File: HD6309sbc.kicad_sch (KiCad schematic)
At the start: 23 parts, among them J1 Conn_01x02_Male, J2 Conn_02x30_Odd_Even, J3 Conn_01x02_Male, U1 HD63C09, U10 74HC375, U11 74HC02, U12 74HC21, U13 74HC21, U4 UM61256FK, U5 UM61256FK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

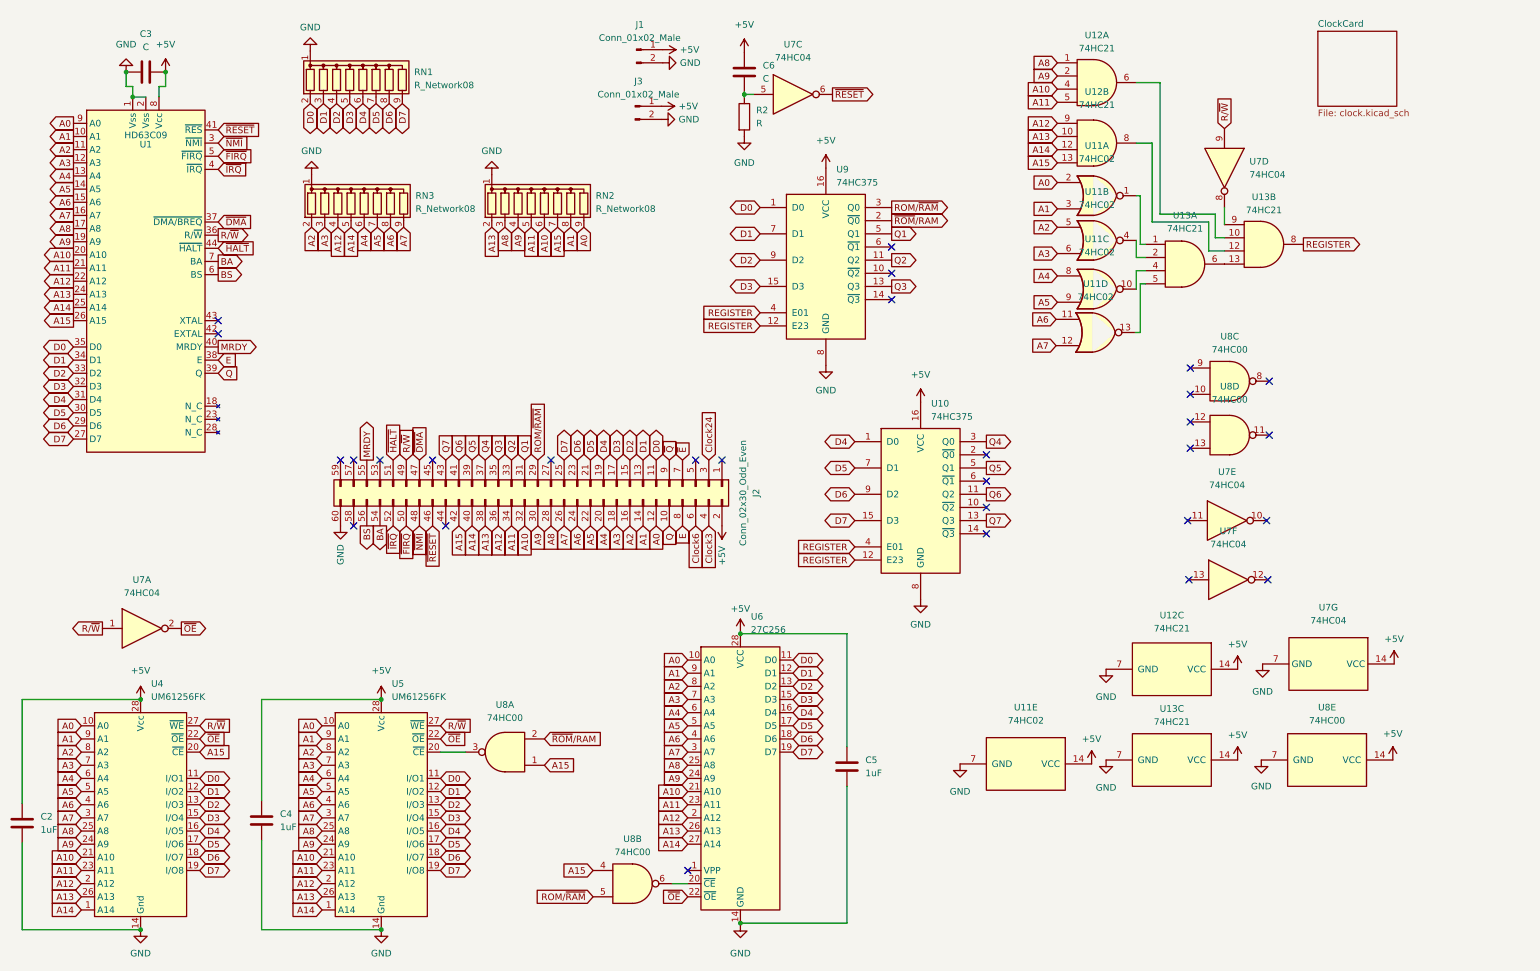
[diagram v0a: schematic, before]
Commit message: add paged memory
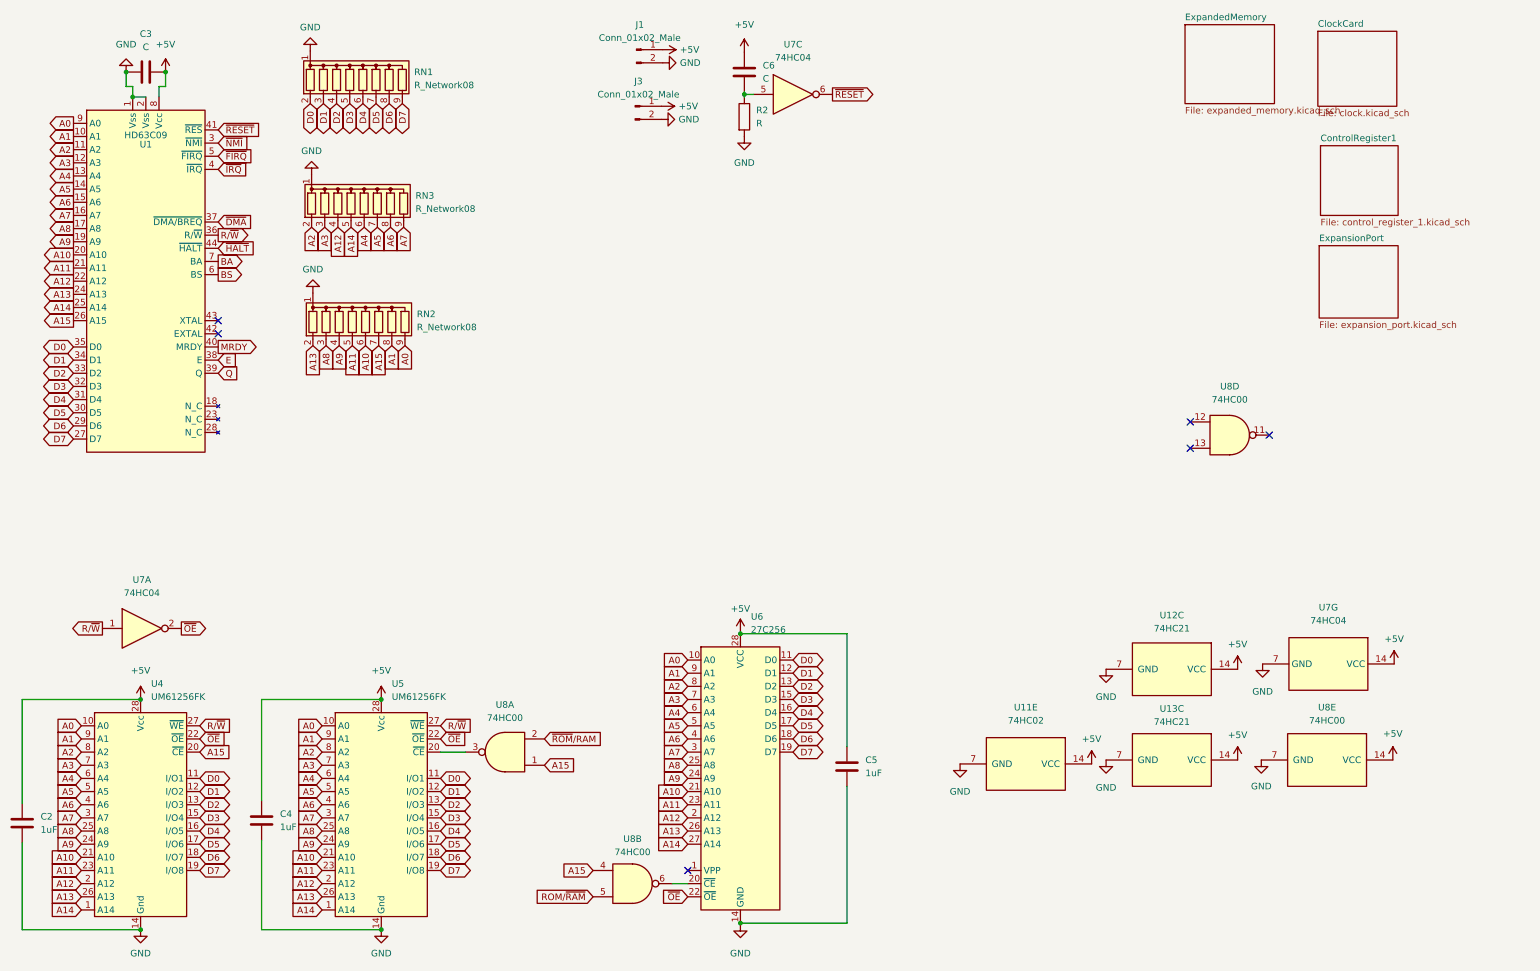
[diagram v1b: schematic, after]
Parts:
- removed J2: Conn_02x30_Odd_Even, Connector_PinHeader_2.54mm:PinHeader_2x30_P2.54mm_Vertical, symbol Connector_Generic:Conn_02x30_Odd_Even
- removed U10, U9: 74HC375, Package_SO:SO-16_3.9x9.9mm_P1.27mm, symbol 74xx:74LS375
- removed unit 4 of U11
- removed unit 3 of U11
- removed unit 1 of U11
- removed unit 2 of U11
- removed unit 1 of U12
- removed unit 2 of U12
- removed unit 2 of U13
- removed unit 1 of U13
- removed unit 5 of U7
- removed unit 6 of U7
- removed unit 4 of U7
- removed unit 3 of U8
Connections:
- no-connect marks 29 -> 6
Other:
- added sheet ControlRegister1 (control_register_1.kicad_sch)
- added sheet ExpandedMemory (expanded_memory.kicad_sch)
- added sheet ExpansionPort (expansion_port.kicad_sch)
- moved on the sheet: RN2

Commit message: add power routing
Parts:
- C3: value C -> 1uF

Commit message: rearrange components for routing
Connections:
- net A0: now also RN3.2 (R1); no longer RN2.9 (R8)
- net A1: now also RN3.3 (R2); no longer RN2.8 (R7)
- net A10: now also RN2.7 (R6); no longer RN2.6 (R5)
- net A11: now also RN2.6 (R5); no longer RN2.5 (R4)
- net A12: now also RN2.5 (R4); no longer RN3.4 (R3)
- net A13: now also RN2.4 (R3); no longer RN2.2 (R1)
- net A14: now also RN2.3 (R2); no longer RN3.5 (R4)
- net A15: now also RN2.2 (R1); no longer RN2.7 (R6)
- net A2: now also RN3.4 (R3); no longer RN3.2 (R1)
- net A3: now also RN3.5 (R4); no longer RN3.3 (R2)
- net A8: now also RN2.9 (R8); no longer RN2.3 (R2)
- net A9: now also RN2.8 (R7); no longer RN2.4 (R3)

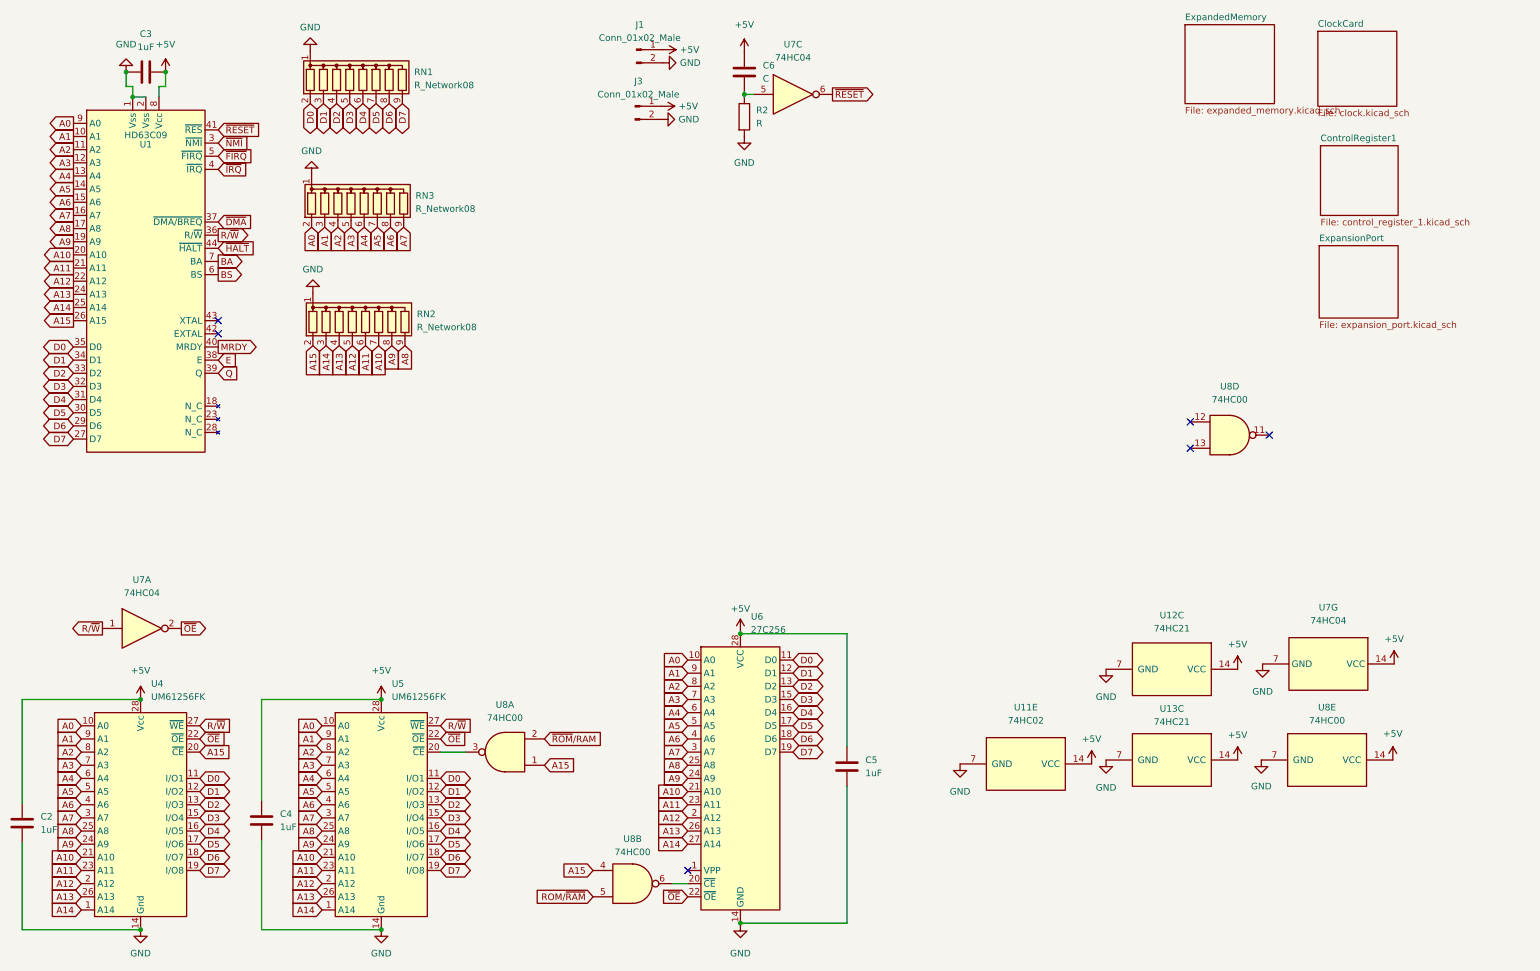
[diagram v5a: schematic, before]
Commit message: move paged memory to external board
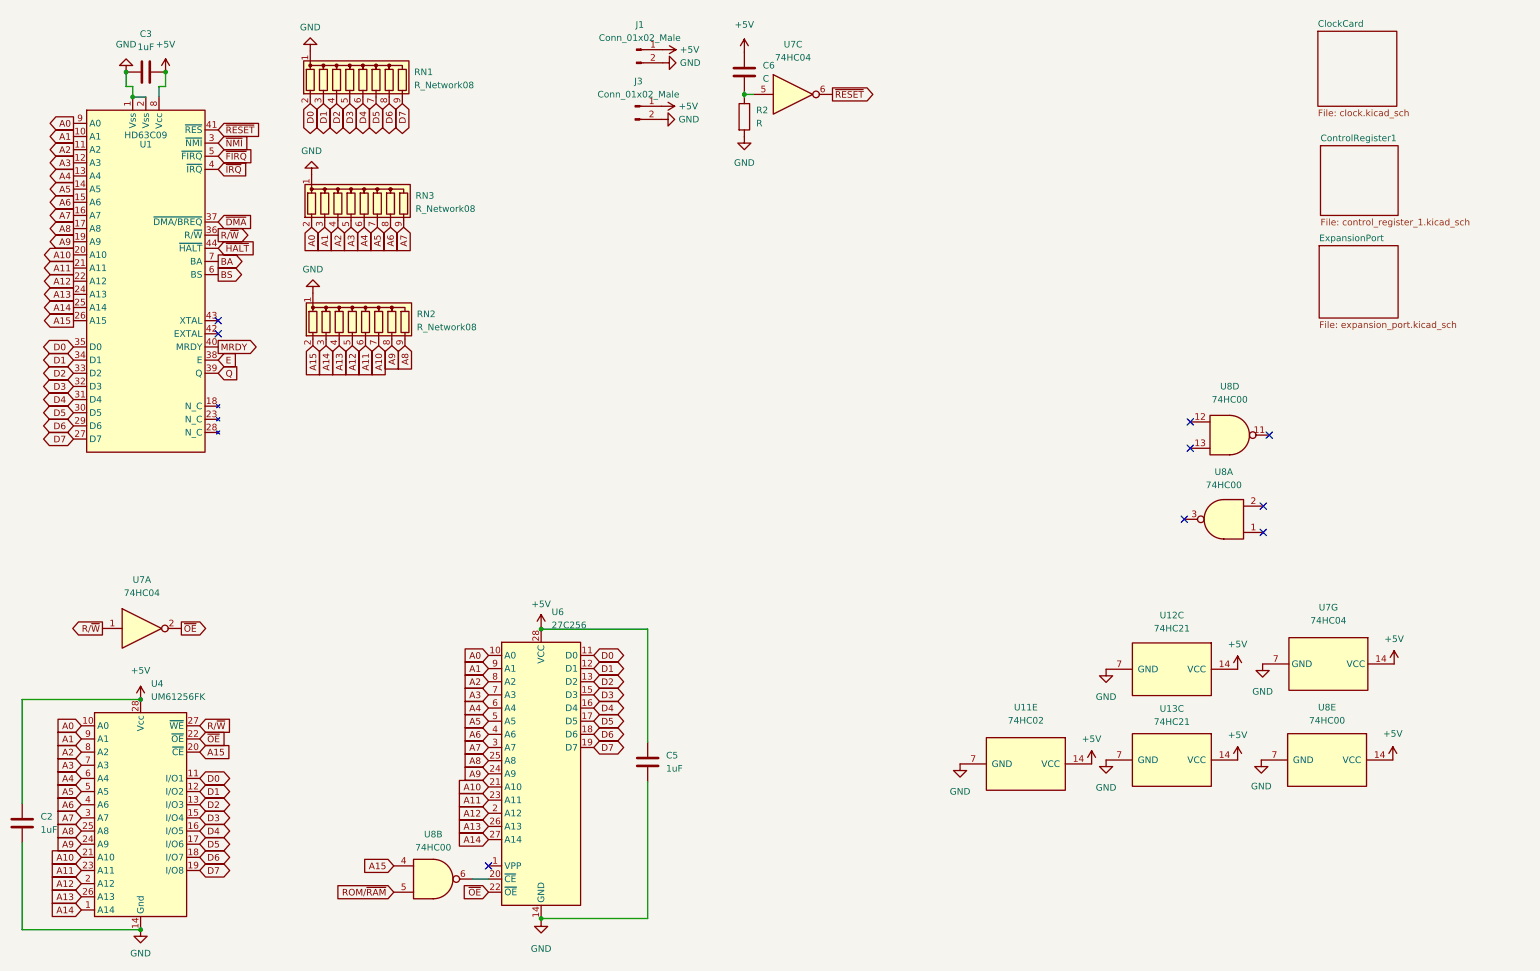
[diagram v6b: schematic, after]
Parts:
- removed C4: 1uF, Capacitor_SMD:C_0805_2012Metric, symbol Device:C
- removed U5: UM61256FK, Package_DIP:DIP-28_W7.62mm, symbol 6309sbc:UM61256FK
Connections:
- net A15: no longer U8.1
- net ~{ROM}/RAM: no longer names the net of U8.2
- no-connect marks 6 -> 9
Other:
- removed sheet ExpandedMemory
- moved on the sheet: C5, U6, U8A, U8B
